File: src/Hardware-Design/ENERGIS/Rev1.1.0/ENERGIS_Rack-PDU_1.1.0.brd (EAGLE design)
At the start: 210 x 108 mm, 432 parts, among them IC1 MP2315GJ-Z, IC10 HLW8032, IC11 HLW8032, IC12 HLW8032, IC13 MP150GJ, IC14 HLW8032, IC15 RP2040, IC16 HLW8032, IC17 MCP6001RT-I/OT, IC18 W25Q128JVPIQ, IC19 CAT24C256HU4IGT3, IC2 MP2315GJ-Z, IC20 W5500, IC21 MIC5504-3.3YM5, IC22 MCP6001RT-I/OT, IC3 ULN2803AFWG, IC4 MCP23017T-E/ML, IC5 MP150GJ, IC6 HLW8032, IC7 HLW8032, IC8 HLW8032, IC9 SN74HC151PWR, J10 0R 1%, J2 JP, J7 JP, J8 0R 1%, J9 0R 1%, K1 G2RL-1A-E DC12, K2 G2RL-1A-E DC12, K3 G2RL-1A-E DC12, K4 G2RL-1A-E DC12, K5 G2RL-1A-E DC12, K6 G2RL-1A-E DC12, K7 G2RL-1A-E DC12, K8 G2RL-1A-E DC12, P12ON Green, P3ON Green, P5ON Green, SW3 TP, X1 ABM8-272-T3 12MHz, X2 25MHz

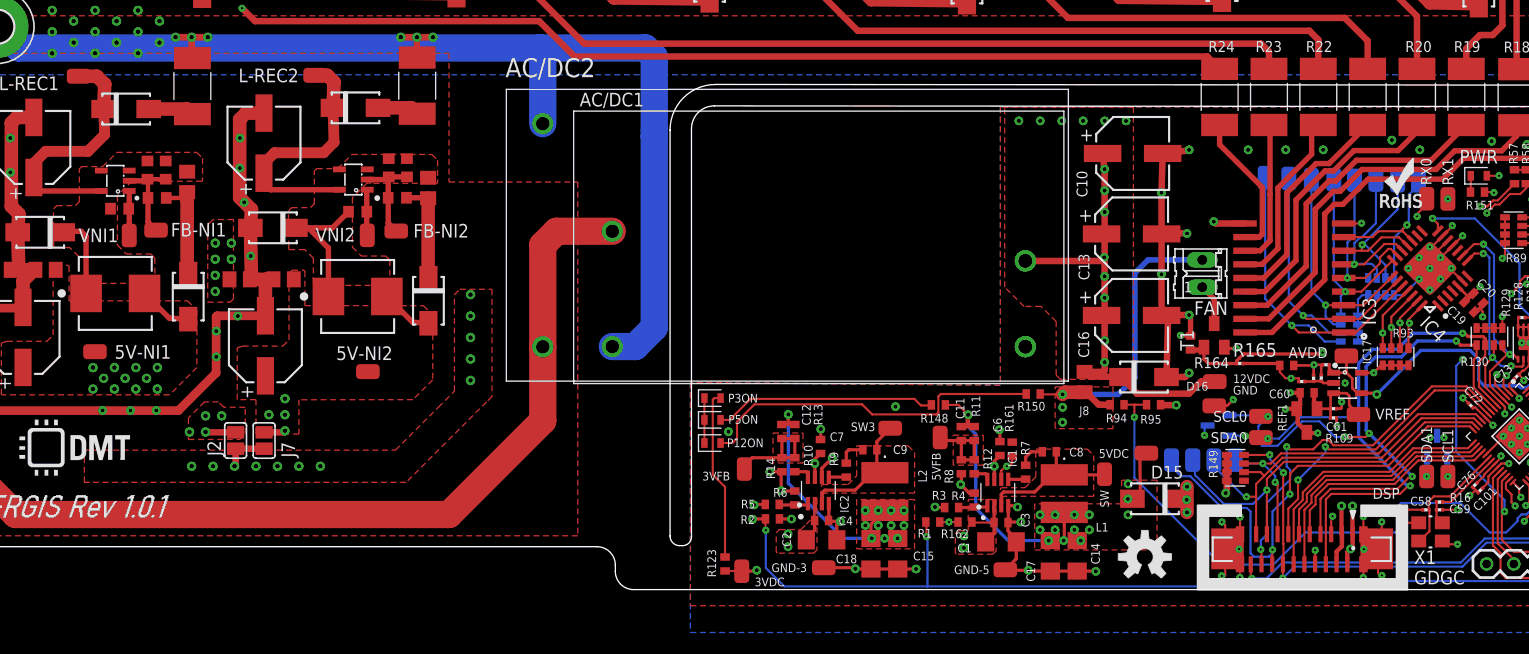
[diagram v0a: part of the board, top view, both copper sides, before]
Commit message: add pcap tests. Small fixes
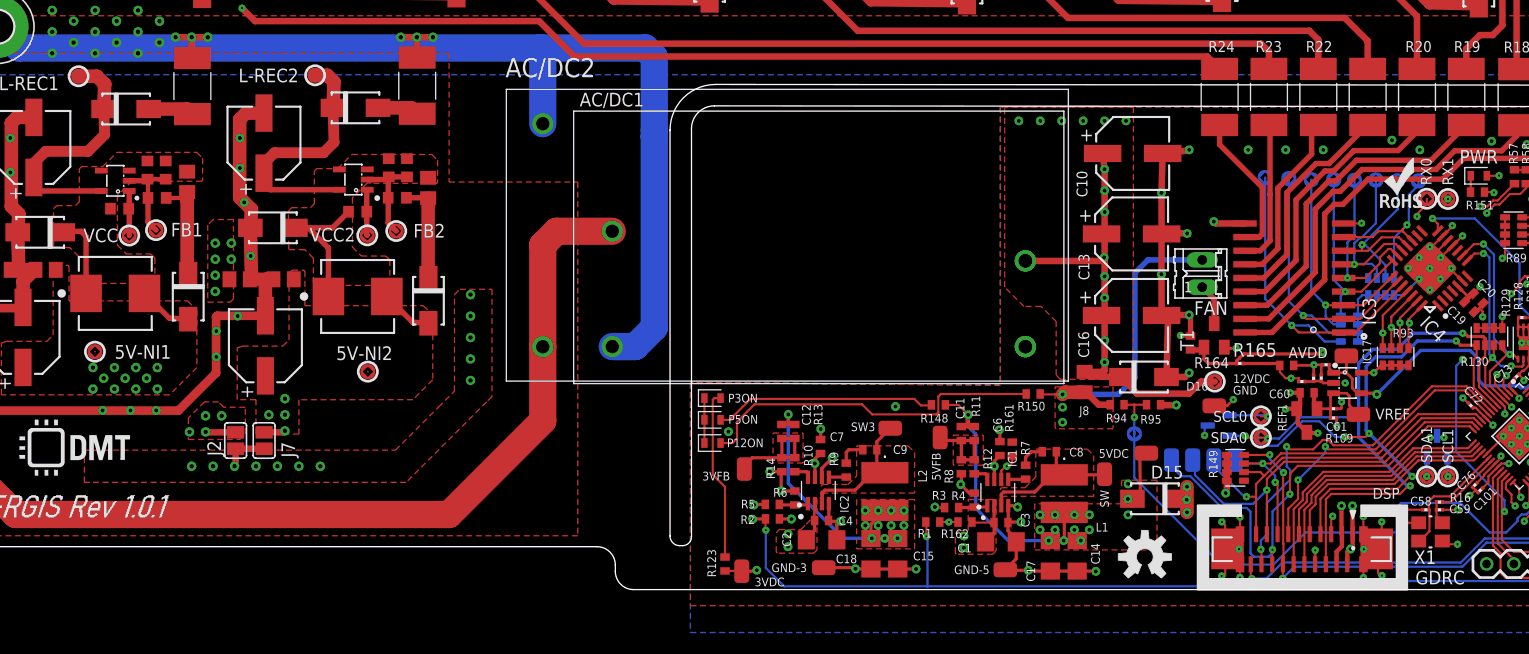
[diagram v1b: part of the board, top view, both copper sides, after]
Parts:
- removed FB-NI1, FB-NI2, VNI1, VNI2: TP, ds_passive:TP
- added ADC12, FB1, FB2, VCC, VCC2: TP-ROUND, ds_passive:TP-ROUND
- 12VDC, 5V-NI1, 5V-NI2, L-REC1, L-REC2, REL0, REL1, REL2, REL3, REL4, REL5, REL6, REL7, RX0, RX1, SCL0, SCL1, SDA0, SDA1: value TP -> TP-ROUND; device ds_passive:TP -> ds_passive:TP-ROUND
- renumbered GDGC to GDRC
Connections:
- net +12V_MEA: now also ADC12.TP
- net FB1: now also FB1.TP; no longer FB-NI1.TP
- net FB2: now also FB2.TP; no longer FB-NI2.TP
- net VNI1: now also VCC.TP; no longer VNI1.TP
- net VNI2: now also VCC2.TP; no longer VNI2.TP

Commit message: adapt design to NextPCB dru
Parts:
- removed CS0, MISO0, MOSI0, SCLK0: TP, ds_passive:TP
- added CS, MI, MO, SC: TP-ROUND, ds_passive:TP-ROUND
- added R166, R167, R168: 3.3K 1%, ds_resistor:0402
- added U$12: (no value), logo:CE_5MM
- added U$13: (no value), SparkFun-Aesthetics:NO_PB_LOGO_0.120
- added U$14: (no value), SparkFun-Aesthetics:ROHS_LOGO_0.18_IN
- added U$15: (no value), ds_silkscreen:SMOKE
- added U$8, U$9: (no value), ds_silkscreen:NEXTPCB
- 3VDC, 3VFB, 5VDC, 5VFB, AVDD, CS1, DVDD, GND, GND-3, GND-5, IOVDD, MISO1, MOSI1, SCLK1, SW, SW3, VBUS, VREF: value TP -> TP-ROUND; device ds_passive:TP -> ds_passive:TP-ROUND
- R130: device ds_resistor:_0603X4-1206 -> ds_resistor:0402
- moved U$7 80.3 mm to (59.0, 42.8)
- moved U$11 57.2 mm to (198.8, 20.6)
- moved U$10 35.9 mm to (129.8, 38.1)
- moved X2 27.6 mm to (193.4, 42.1), turned to 0 degrees
- moved C87 25.3 mm to (194.7, 39.9), turned to 0 degrees
- moved R144 24.7 mm to (193.4, 39.9), turned to 180 degrees
- moved C84 24.1 mm to (199.8, 35.5), turned to 0 degrees
- moved C86 24.1 mm to (192.1, 39.9), turned to 180 degrees
- moved C88 23.9 mm to (194.5, 39.0), turned to 180 degrees
- moved C85 23.5 mm to (200.7, 33.9), turned to 0 degrees
- moved C95 23.4 mm to (199.8, 34.8), turned to 0 degrees
- moved RGTG 23.1 mm to (182.2, 22.0), turned to 90 degrees
- moved R130 21.9 mm to (137.6, 9.11), turned to 270 degrees
- moved SCLK1 21.5 mm to (203.7, 40.9), turned to 0 degrees
- moved C94 21.0 mm to (199.7, 32.3), turned to 270 degrees
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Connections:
- net +3V3_MCU: now also R130.1, R166.1, R167.1, R168.1; no longer R130.A2, R130.B2, R130.C2, R130.D2
- net I2C0_SCL: now also R130.2; no longer R130.A1
- net I2C0_SDA: now also R166.2; no longer R130.B1
- net I2C1_SCL: now also D18.2, R167.2; no longer D18.1, R130.C1
- net I2C1_SDA: now also D18.1, R168.2; no longer D18.2, R130.D1
- net LCD_CS: now also CS.TP; no longer CS0.TP
- net LCD_MISO: now also MI.TP; no longer MISO0.TP
- net LCD_MOSI: now also MO.TP; no longer MOSI0.TP
- net LCD_SCLK: now also SC.TP; no longer SCLK0.TP
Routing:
- net SH: track 134.5 -> 78.4 mm, vias 1 -> 3
- net UART0_TX: track 100.4 -> 59.0 mm
- net UART0_RX: track 97.4 -> 56.6 mm, vias 4 -> 6
- net +3V3_MCU: track 124.4 -> 91.5 mm, vias 19 -> 27
- net RUN: track 83.6 -> 52.2 mm
- net I2C0_SCL: track 62.2 -> 34.4 mm, vias 5 -> 3
- net GND: track 292.2 -> 269.3 mm, vias 160 -> 720
- net I2C0_SDA: track 61.4 -> 40.4 mm, vias 4 -> 3
- net BUCK_EN: track 121.6 -> 100.9 mm, vias 5 -> 6
- net !QSPI_SS: track 51.4 -> 31.2 mm, vias 2 -> 3
- net W5500_MISO: track 55.0 -> 70.8 mm, vias 3 -> 5
- net W5500_SCK: track 53.8 -> 68.7 mm
- net +12V: track 395.1 -> 380.8 mm, vias 9 -> 13
- net !LINK: track 34.2 -> 20.1 mm
- net !W5500_CS: track 61.5 -> 75.6 mm
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- added copper zone on layer 14, net +12V
- added copper zone on layer 14, net +3V3
- added copper zone on layer 14, net +3V3_A
- added copper zone on layer 14, net +3V3_MCU
- added copper zone on layer 14, net 12VRAW
- added copper zone on layer 3, net GND
- added copper zone on layer 16, net SH
- removed copper zone on layer 3, net +3V3
- removed copper zone on layer 3, net +3V3_A
- removed copper zone on layer 3, net +3V3_MCU
- removed copper zone on layer 3, net 12VRAW
- removed copper zone on layer 14, net GND
- removed copper zone on layer 1, net SH
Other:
- outline, holes or cut-outs redrawn
- board text added: "L"
- board text added: "N"

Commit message: update version to 1.1.0
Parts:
- moved C88 0.19 mm to (194.5, 39.2)
- moved C65 0.18 mm to (171.1, 10.00)
- moved C74 0.16 mm to (162.8, 15.6)
- moved C90 0.15 mm to (187.3, 32.9)
- moved C89 0.15 mm to (187.3, 31.9)
- moved C70 0.15 mm to (162.2, 16.1)
- moved C75 0.15 mm to (161.7, 16.7)
- moved R121 0.13 mm to (178.2, 5.28)
- moved C67 0.12 mm to (168.0, 25.0)
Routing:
- net GND: track 269.3 -> 273.1 mm
- net AVDD: track 34.9 -> 32.5 mm
- net QSPI_SD1: track 8.99 -> 9.80 mm
- net +3V3: track 97.0 -> 96.4 mm
- net MCP_REL_RST: track 37.7 -> 38.3 mm
- net QSPI_SD0: track 12.9 -> 13.4 mm
- net W5500_MISO: track 70.8 -> 70.2 mm
- net +3V3_MCU: track 91.5 -> 92.1 mm
- net QSPI_SD3: track 16.6 -> 17.1 mm

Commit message: update component library to NextPCB
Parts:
- 12VDC, 3VDC, 3VFB, 5V-NI1, 5V-NI2, 5VDC, 5VFB, ADC12, AVDD, CS, CS1, DVDD, FB1, FB2, GND, GND-3, GND-5, IOVDD, L-REC1, L-REC2, MI, MISO1, MO, MOSI1, REL0, REL1, REL2, REL3, REL4, REL5, REL6, REL7, RX0, RX1, SC, SCL0, SCL1, SCLK1, SDA0, SDA1, SW, SW3, VBUS, VCC, VCC2, VREF: value TP-ROUND -> TESTPOINT
- IC9: value SN74HC151PWR -> CD74ACT151M96
- REF1: value LM4040B30FTA -> LM4040x30

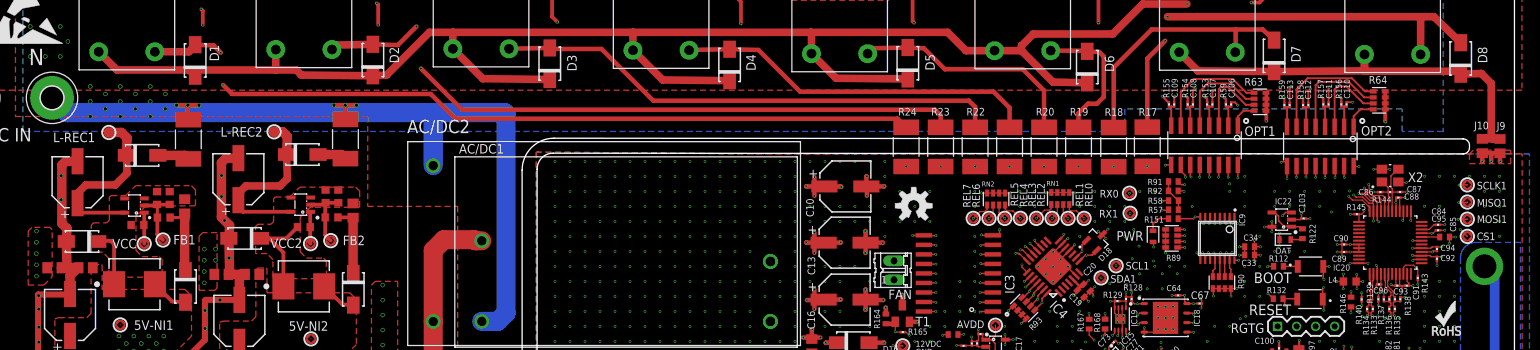
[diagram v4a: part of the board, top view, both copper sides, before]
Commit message: update component library to NextPCB
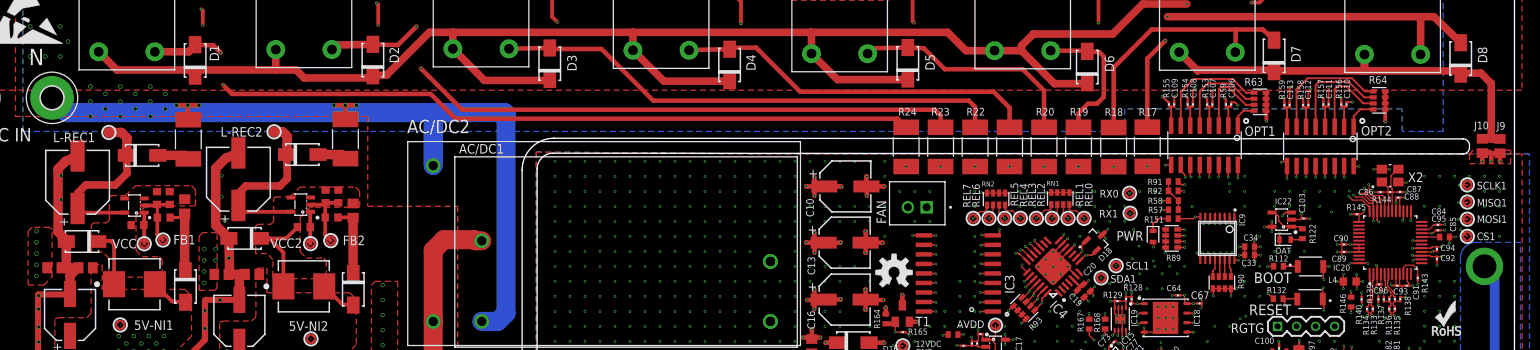
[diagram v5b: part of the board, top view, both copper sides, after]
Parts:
- AC/DC2: value IRM-10-15 -> DNI
- AC_L, AC_N: value MOUNT-PAD-ROUND3.0 -> DNI
- C35, C47: value 2.2uF 400V -> 2.2uF 400v; device ds_capacitors:6.3X7.7(DXL) -> ds_capacitors:8X10.5(DXL)
- C65, C97, C99: value 10uF 50V -> 22uF 25V
- C83: device ds_passive:C1206 -> ds_capacitors:1206
- FAN: device con-amp-quick:02P -> ds_con:B2B-XH-A
- GDRC, RGTG, U$1, U$10, U$11, U$12, U$13, U$14, U$15, U$2, U$3, U$4, U$5, U$6, U$7, U$8, U$9: value (none) -> DNI
- J2, J7: value JP -> DNI
- L1: value 4.9uH -> 4.7uH; device ds_passive:SRR5228A -> ds_inductor:SRR5228A
- L2: value 4.2uH -> 4.7uH; device ds_passive:SRR5228A -> ds_inductor:SRR5228A
- L_OUT1, L_OUT2, L_OUT3, L_OUT4, L_OUT5, L_OUT6, L_OUT7, L_OUT8, N_OUT1, N_OUT2, N_OUT3, N_OUT4, N_OUT5, N_OUT6, N_OUT7, N_OUT8: value MOUNT-PAD-ROUND2.8 -> DNI
- R10: value 33K -> 33K 1%; device ds_passive:0402 -> ds_resistor:0402
- R128, R165: value NC -> DNI
- R143: device ds_passive:R0201 -> ds_resistor:0201
- T1: value (none) -> BSS138
- moved FAN 9.46 mm to (130.3, 38.4), turned to 0 degrees
- moved U$10 9.28 mm to (127.2, 29.2)
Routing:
- net N$23: track 4.09 -> 14.5 mm
- net +12V: track 380.8 -> 385.7 mm
- net AGND: track 351.5 -> 353.1 mm
- net LREC1: track 23.7 -> 24.3 mm
- net GND: vias 720 -> 716

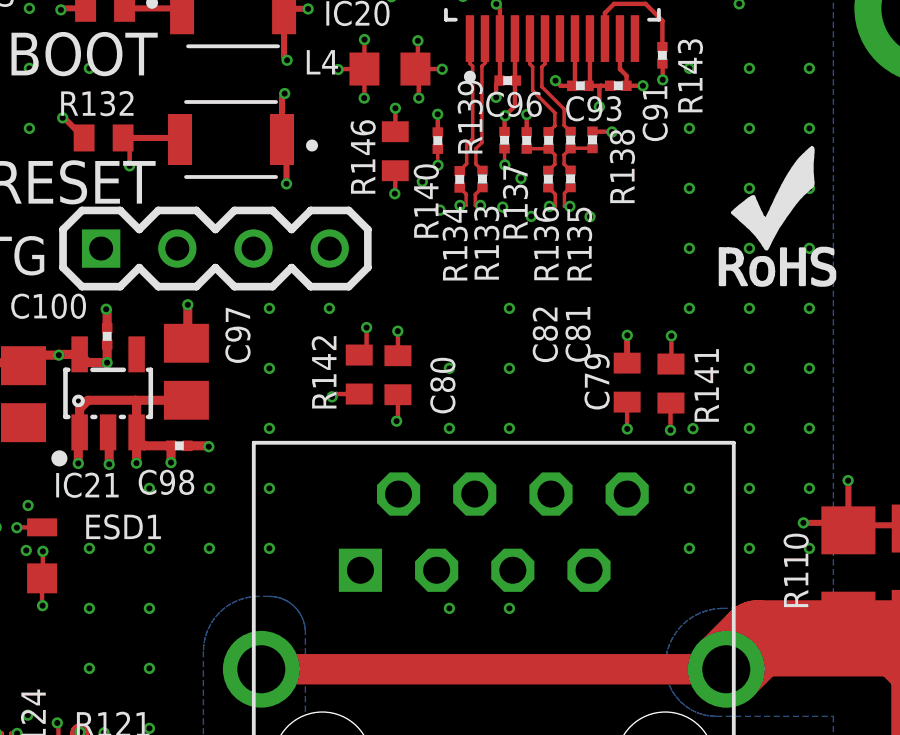
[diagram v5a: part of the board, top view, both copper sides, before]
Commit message: generate PCB reports
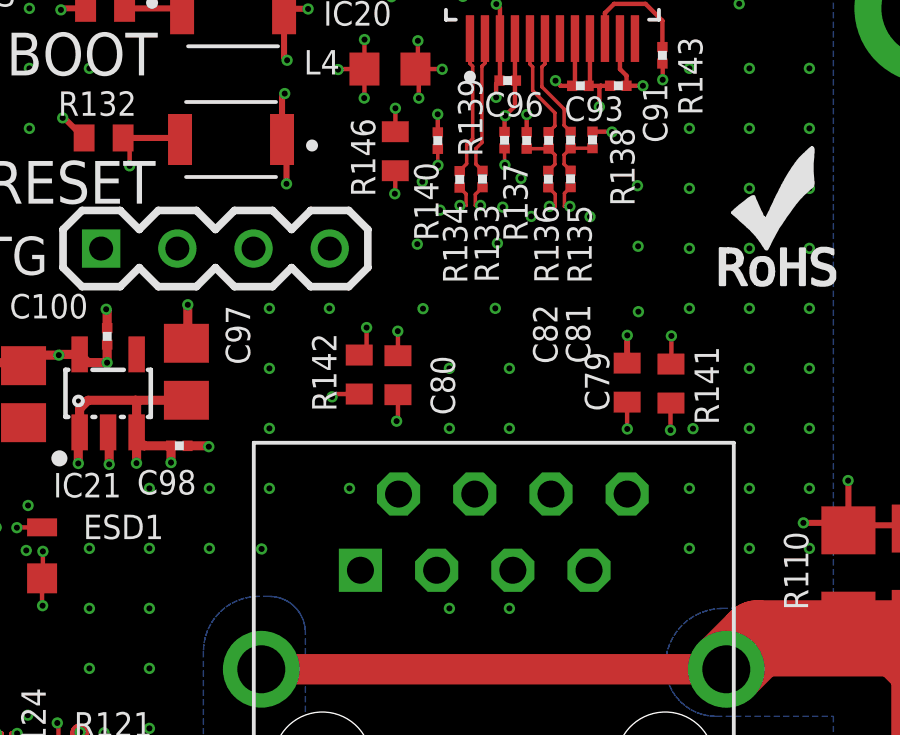
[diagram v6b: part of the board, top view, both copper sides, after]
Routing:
- net RD_N: track 16.1 -> 27.3 mm
- net RD_P: track 17.1 -> 27.3 mm
- net USB2_DP_N: track 32.6 -> 35.4 mm
- net TD_P: track 24.8 -> 27.5 mm
- net USB2_DP_P: track 33.4 -> 35.4 mm
- net TD_N: track 26.0 -> 27.5 mm
- net GND: vias 716 -> 723
